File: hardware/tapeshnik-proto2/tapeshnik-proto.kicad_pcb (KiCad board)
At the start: 2 copper layers, 84.3 x 64.5 mm, 132 parts, among them J1 Conn_01x02, J10 Conn_01x09, J2 RW_HEAD, J3 Conn_01x07, J4 ERASERHEAD, J5 RW_HEAD, J6 Conn_01x01_Pin, J7 Conn_01x01_Pin, J8 Conn_01x01_Pin, J9 Conn_01x01_Pin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

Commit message: kicad files for the mecha and motor controller
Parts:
- C1, C11, C15, C22, C5: value 0.1 -> 0.1u
- C10, C16, C19, C20, C8, C9: value 0.1uF -> 0.1u
- C17: value 10.0/10V -> 10.0u/25V
- C18: value 10.0u/16V -> 10.0u/25V
- C21, C6, C7: value 10.0u/10V -> 10.0u/25V
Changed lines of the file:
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@@
         (effects (font (size 0.7 0.7) (thickness 0.15)))
     )
-    (fp_text value "0.1uF" (at 0 1.43 90) (layer "F.Fab")
+    (fp_text value "0.1u" (at 0 1.43 90) (layer "F.Fab")
         (effects (font (size 1 1) (thickness 0.15)))
     )
@@
         (effects (font (size 0.7 0.7) (thickness 0.15)))
     )
-    (fp_text value "0.1" (at 0 1.68) (layer "F.Fab")
+    (fp_text value "0.1u" (at 0 1.68) (layer "F.Fab")
         (effects (font (size 1 1) (thickness 0.15)))
     )
@@
         (effects (font (size 0.7 0.7) (thickness 0.15)))
     )
-    (fp_text value "10.0u/10V" (at 0 1.68) (layer "F.Fab")
+    (fp_text value "10.0u/25V" (at 0 1.68) (layer "F.Fab")
         (effects (font (size 1 1) (thickness 0.15)))
     )
@@
         (effects (font (size 0.7 0.7) (thickness 0.15)))
     )
-    (fp_text value "10.0/10V" (at 0 1.68 90) (layer "F.Fab")
+    (fp_text value "10.0u/25V" (at 0 1.68 90) (layer "F.Fab")
         (effects (font (size 1 1) (thickness 0.15)))
     )
@@
     (descr "Capacitor SMD 0805 (2012 Metric), square (rectangular) end terminal, IPC_7351 nominal, (Body size source: IPC-SM-782 page 76, https://www.pcb-3d.com/wordpress/wp-content/uploads/ipc-sm-782a_amendment_1_and_2.pdf, https://docs.google.com/spreadsheets/d/1BsfQQcO9C6DZCsRaXUlFlo91Tg2WpOkGARC1WS5S8t0/edit?usp=sharing), generated with kicad-footprint-generator")
     (tags "capacitor")
+    (property "LCSC" "C49678")
     (property "Sheetfile" "tapeshnik-proto.kicad_sch")
     (property "Sheetname" "")
@@
         (effects (font (size 0.7 0.7) (thickness 0.15)))
     )
-    (fp_text value "0.1" (at 0 1.68) (layer "F.Fab")
+    (fp_text value "0.1u" (at 0 1.68) (layer "F.Fab")
         (effects (font (size 1 1) (thickness 0.15)))
     )
@@
         (effects (font (size 0.7 0.7) (thickness 0.15)))
     )
-    (fp_text value "0.1uF" (at 0 1.43 90) (layer "F.Fab")
+    (fp_text value "0.1u" (at 0 1.43 90) (layer "F.Fab")
         (effects (font (size 1 1) (thickness 0.15)))
     )
@@
         (effects (font (size 0.7 0.7) (thickness 0.15)))
     )
-    (fp_text value "10.0u/16V" (at 0 1.68 90) (layer "F.Fab")
+    (fp_text value "10.0u/25V" (at 0 1.68 90) (layer "F.Fab")
         (effects (font (size 1 1) (thickness 0.15)))
     )
@@
         (effects (font (size 0.7 0.7) (thickness 0.15)))
     )
-    (fp_text value "0.1uF" (at 0 1.43 90) (layer "F.Fab")
+    (fp_text value "0.1u" (at 0 1.43 90) (layer "F.Fab")
         (effects (font (size 1 1) (thickness 0.15)))
     )
@@
         (effects (font (size 0.7 0.7) (thickness 0.15)))
     )
-    (fp_text value "10.0u/10V" (at 0 1.68) (layer "F.Fab")
+    (fp_text value "10.0u/25V" (at 0 1.68) (layer "F.Fab")
         (effects (font (size 1 1) (thickness 0.15)))
     )
@@
         (effects (font (size 0.7 0.7) (thickness 0.15)))
     )
-    (fp_text value "10.0u/10V" (at 0 1.68) (layer "F.Fab")
+    (fp_text value "10.0u/25V" (at 0 1.68) (layer "F.Fab")
         (effects (font (size 1 1) (thickness 0.15)))
     )
@@
         (effects (font (size 0.7 0.7) (thickness 0.15)))
     )
-    (fp_text value "0.1uF" (at 0 1.43) (layer "F.Fab")
+    (fp_text value "0.1u" (at 0 1.43) (layer "F.Fab")
         (effects (font (size 1 1) (thickness 0.15)))
     )
@@
         (effects (font (size 0.7 0.7) (thickness 0.15)))
     )
-    (fp_text value "0.1uF" (at 0 1.43) (layer "F.Fab")
+    (fp_text value "0.1u" (at 0 1.43) (layer "F.Fab")
         (effects (font (size 1 1) (thickness 0.15)))
     )
@@
         (effects (font (size 0.7 0.7) (thickness 0.15)))
     )
-    (fp_text value "0.1uF" (at 0 1.43 90) (layer "F.Fab")
+    (fp_text value "0.1u" (at 0 1.43 90) (layer "F.Fab")
         (effects (font (size 1 1) (thickness 0.15)))
     )
@@
         (effects (font (size 0.7 0.7) (thickness 0.15)))
     )
-    (fp_text value "0.1" (at 0 1.68 90) (layer "F.Fab")
+    (fp_text value "0.1u" (at 0 1.68 90) (layer "F.Fab")
         (effects (font (size 1 1) (thickness 0.15)))
     )
@@
         (effects (font (size 0.7 0.7) (thickness 0.15)))
     )
-    (fp_text value "0.1" (at 0 1.68 90) (layer "F.Fab")
+    (fp_text value "0.1u" (at 0 1.68 90) (layer "F.Fab")
         (effects (font (size 1 1) (thickness 0.15)))
     )
@@
         (effects (font (size 0.7 0.7) (thickness 0.15)))
     )
-    (fp_text value "0.1" (at 0 1.68) (layer "F.Fab")
+    (fp_text value "0.1u" (at 0 1.68) (layer "F.Fab")
         (effects (font (size 1 1) (thickness 0.15)))
     )

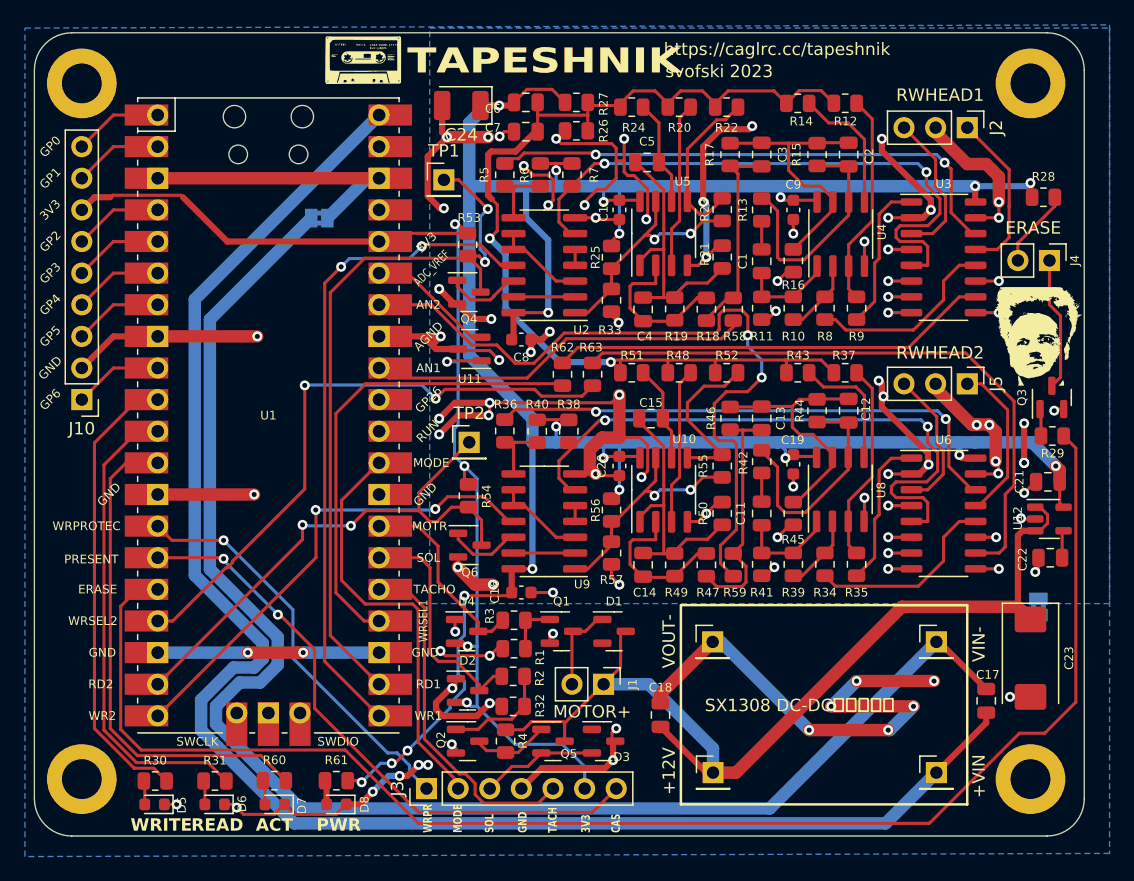
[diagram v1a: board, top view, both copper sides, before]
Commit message: updated schematics
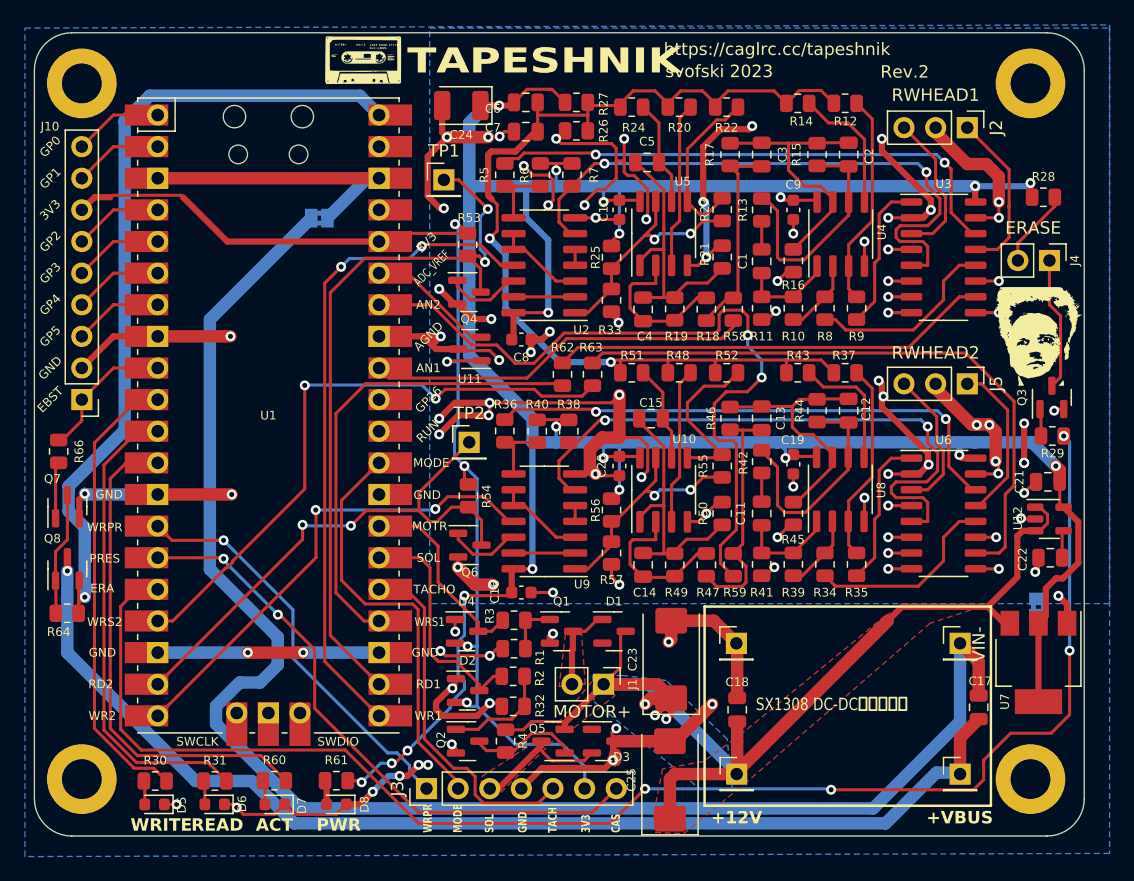
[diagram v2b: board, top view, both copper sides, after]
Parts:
- added C25: 220.0/16V, Capacitor_Tantalum_SMD:CP_EIA-7343-31_Kemet-D, F.Cu at (197.1, 96.6)
- added Q7: S8050, Package_TO_SOT_SMD:SOT-23, F.Cu at (148.7, 74.6)
- added Q8: AO3401, Package_TO_SOT_SMD:SOT-23, F.Cu at (148.7, 79.6)
- added R64: 22K, Resistor_SMD:R_0805_2012Metric, F.Cu at (148.7, 83.2)
- added R66: 4K7, Resistor_SMD:R_0805_2012Metric, F.Cu at (148.0, 70.2)
- added U7: AMS1117-5.0, Package_TO_SOT_SMD:SOT-223-3_TabPin2, F.Cu at (226.7, 87.2)
- C13, C3: value 2000p -> 2200p
- Q5: value AP3101 -> AO3401
- R61: value 760 -> 680
- moved C23 28.9 mm to (197.2, 86.9), turned to 90 degrees
- moved C18 6.17 mm to (202.5, 91.0)
- moved J8 1.91 mm to (202.4, 85.6)
- moved J6 1.91 mm to (220.4, 96.1)
- moved J7 1.91 mm to (220.4, 85.6)
- moved J9 1.91 mm to (202.5, 96.1)
- moved C17 0.80 mm to (221.9, 90.8)
- turned Q5 to 180 degrees
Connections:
- net Net-(J10-Pin_1) renamed /EBOOST
- C17 pad 1: /VBUS -> /VBUSSEQ
- J6 pad 1: /VBUS -> /VBUSSEQ
- Q5 pad 2: /CAS_SOL -> +12V
- Q5 pad 3: +12V -> /CAS_SOL
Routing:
- net /VBUSSEQ: track 0.00 -> 91.8 mm, vias 0 -> 1
- net /VBUS: track 131.4 -> 66.8 mm, vias 0 -> 1
- net +12V: track 75.2 -> 93.7 mm, vias 0 -> 3
- net GNDD: track 156.1 -> 138.2 mm, vias 26 -> 22
- net +5V: track 225.1 -> 242.9 mm
- net Net-(Q7-C): track 0.00 -> 9.90 mm
- net Net-(J7-Pin_1): track 121.1 -> 126.0 mm
- net Net-(Q7-B): track 0.00 -> 4.83 mm
- net /EBOOST: track 7.15 -> 10.9 mm
- net Net-(Q2-D): track 6.24 -> 8.91 mm
- net GND: track 222.8 -> 225.3 mm, vias 73 -> 74
- net /CAS_SOL: track 9.14 -> 10.6 mm
- net /CAS_ERASE: track 119.1 -> 119.9 mm, vias 0 -> 4
- net /CAS_MODE: track 35.1 -> 35.8 mm
- added copper zone on B.Cu, net +12V
- added copper zone on F.Cu, net +12V
- added copper zone on F.Cu, net /CAS_SOL
- added copper zone on F.Cu, net Net-(D1-A)
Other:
- board text added: "+VBUS"
- board text added: "Rev.2"
- board text removed: "+VIN"
- board text removed: "VOUT-"
